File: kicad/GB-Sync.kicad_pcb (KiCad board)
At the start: 2 copper layers, 18.1 x 18.1 mm, 4 parts

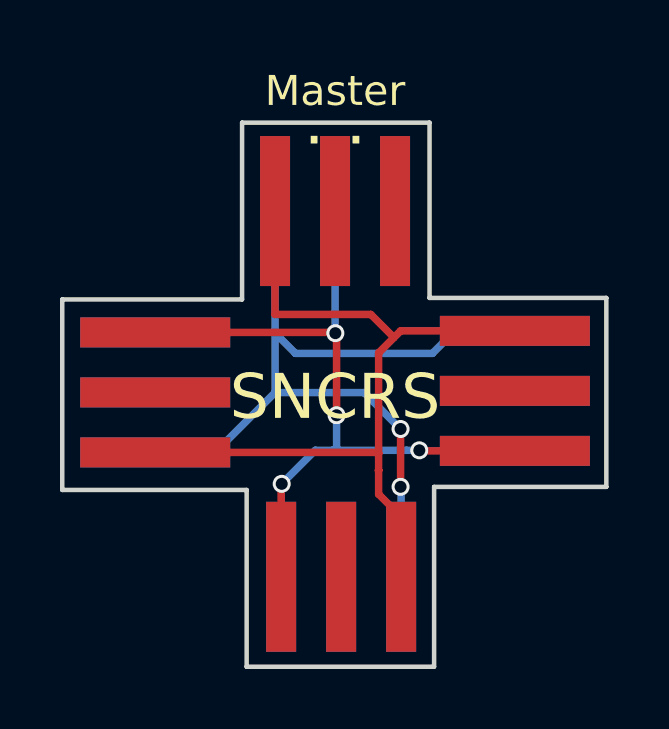
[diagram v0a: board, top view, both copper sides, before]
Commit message: Added more info in the front silkscreen and geeky info in the back
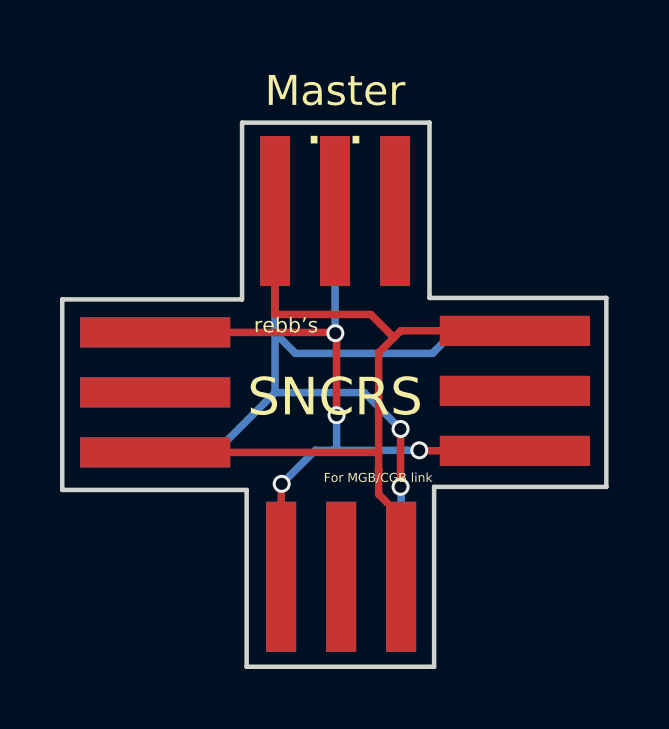
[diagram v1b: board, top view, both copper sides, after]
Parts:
- added G***: tplogo, gb_link:twinpeaks, B.Cu at (149.9, 100.3)
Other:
- board text added: "For MGB/CGB link"
- board text added: "Lesbinary 2018/09"
- board text added: "rebb’s"
